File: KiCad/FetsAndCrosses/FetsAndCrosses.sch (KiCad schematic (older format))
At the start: 0 parts

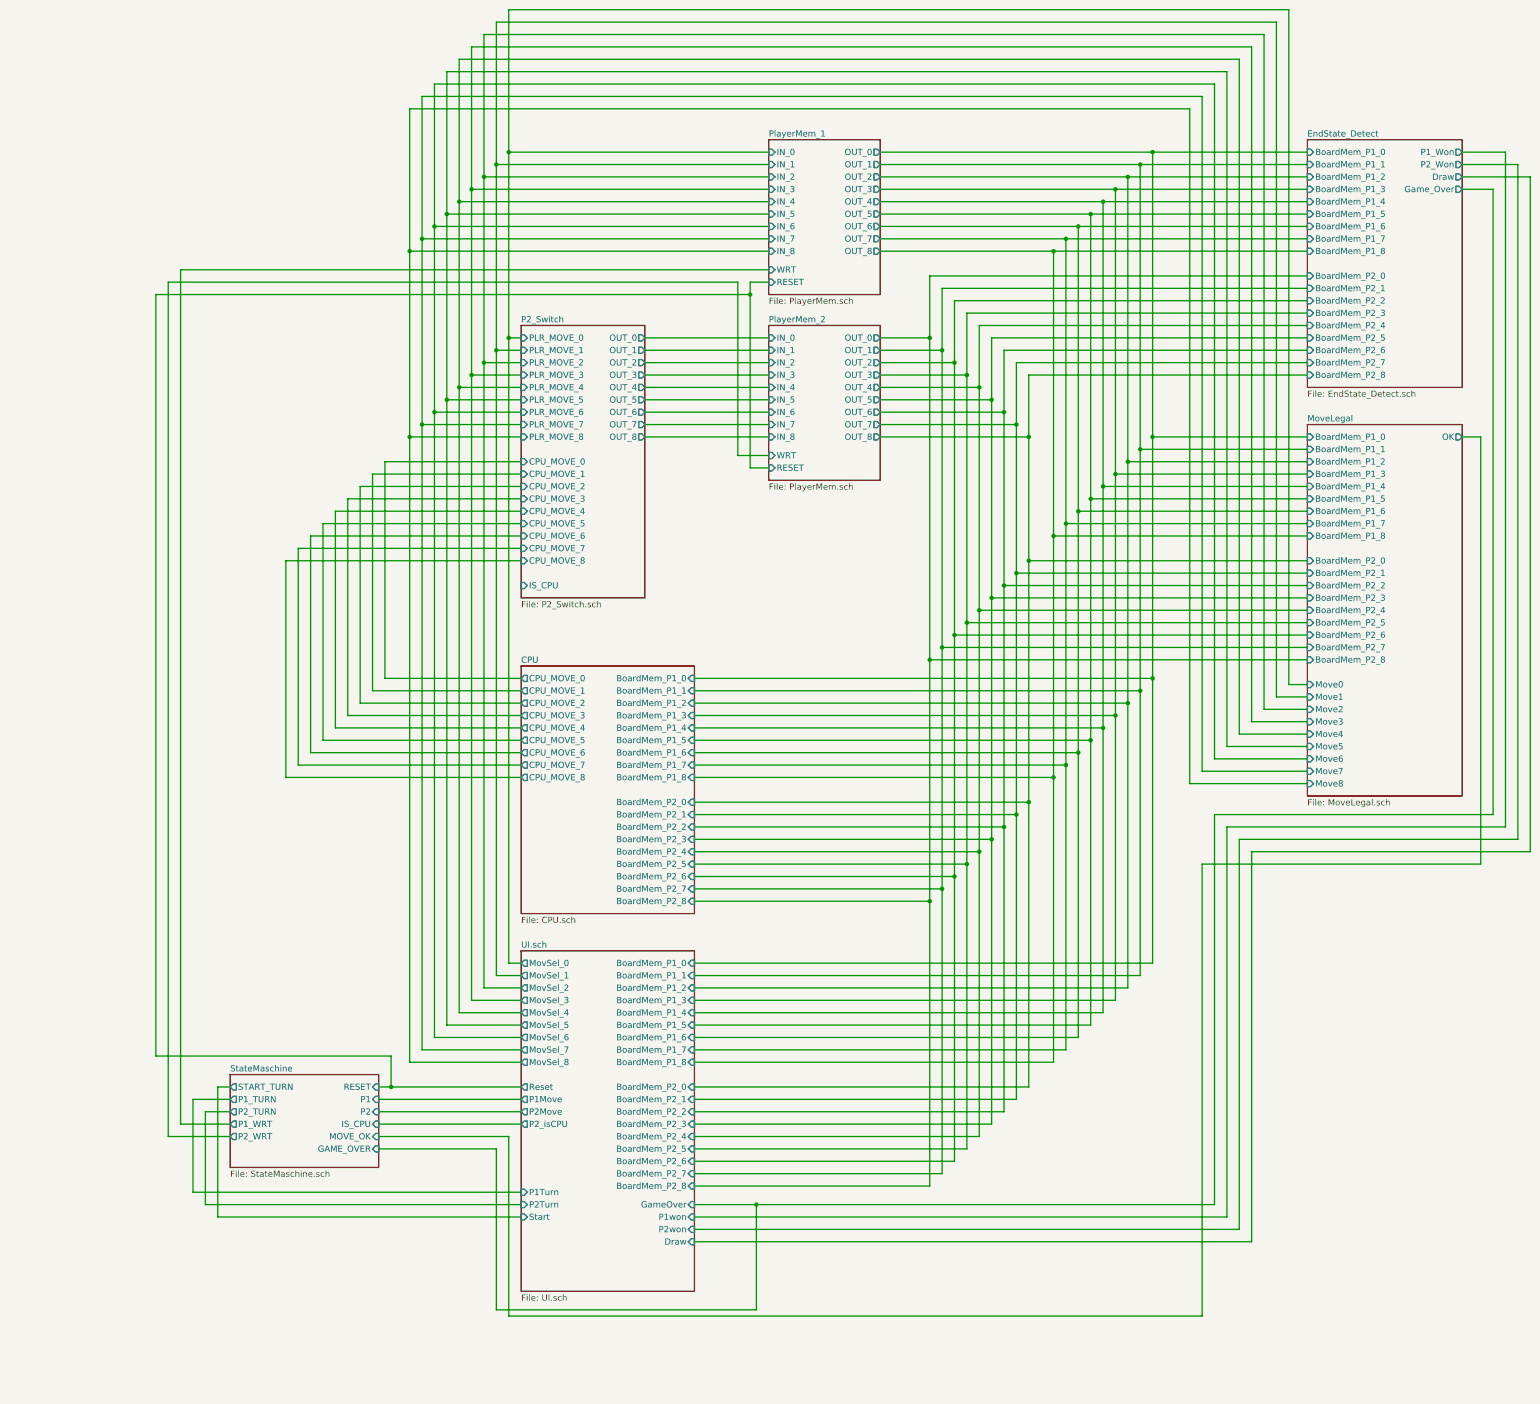
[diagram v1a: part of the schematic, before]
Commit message: Reworked everything to use Buses
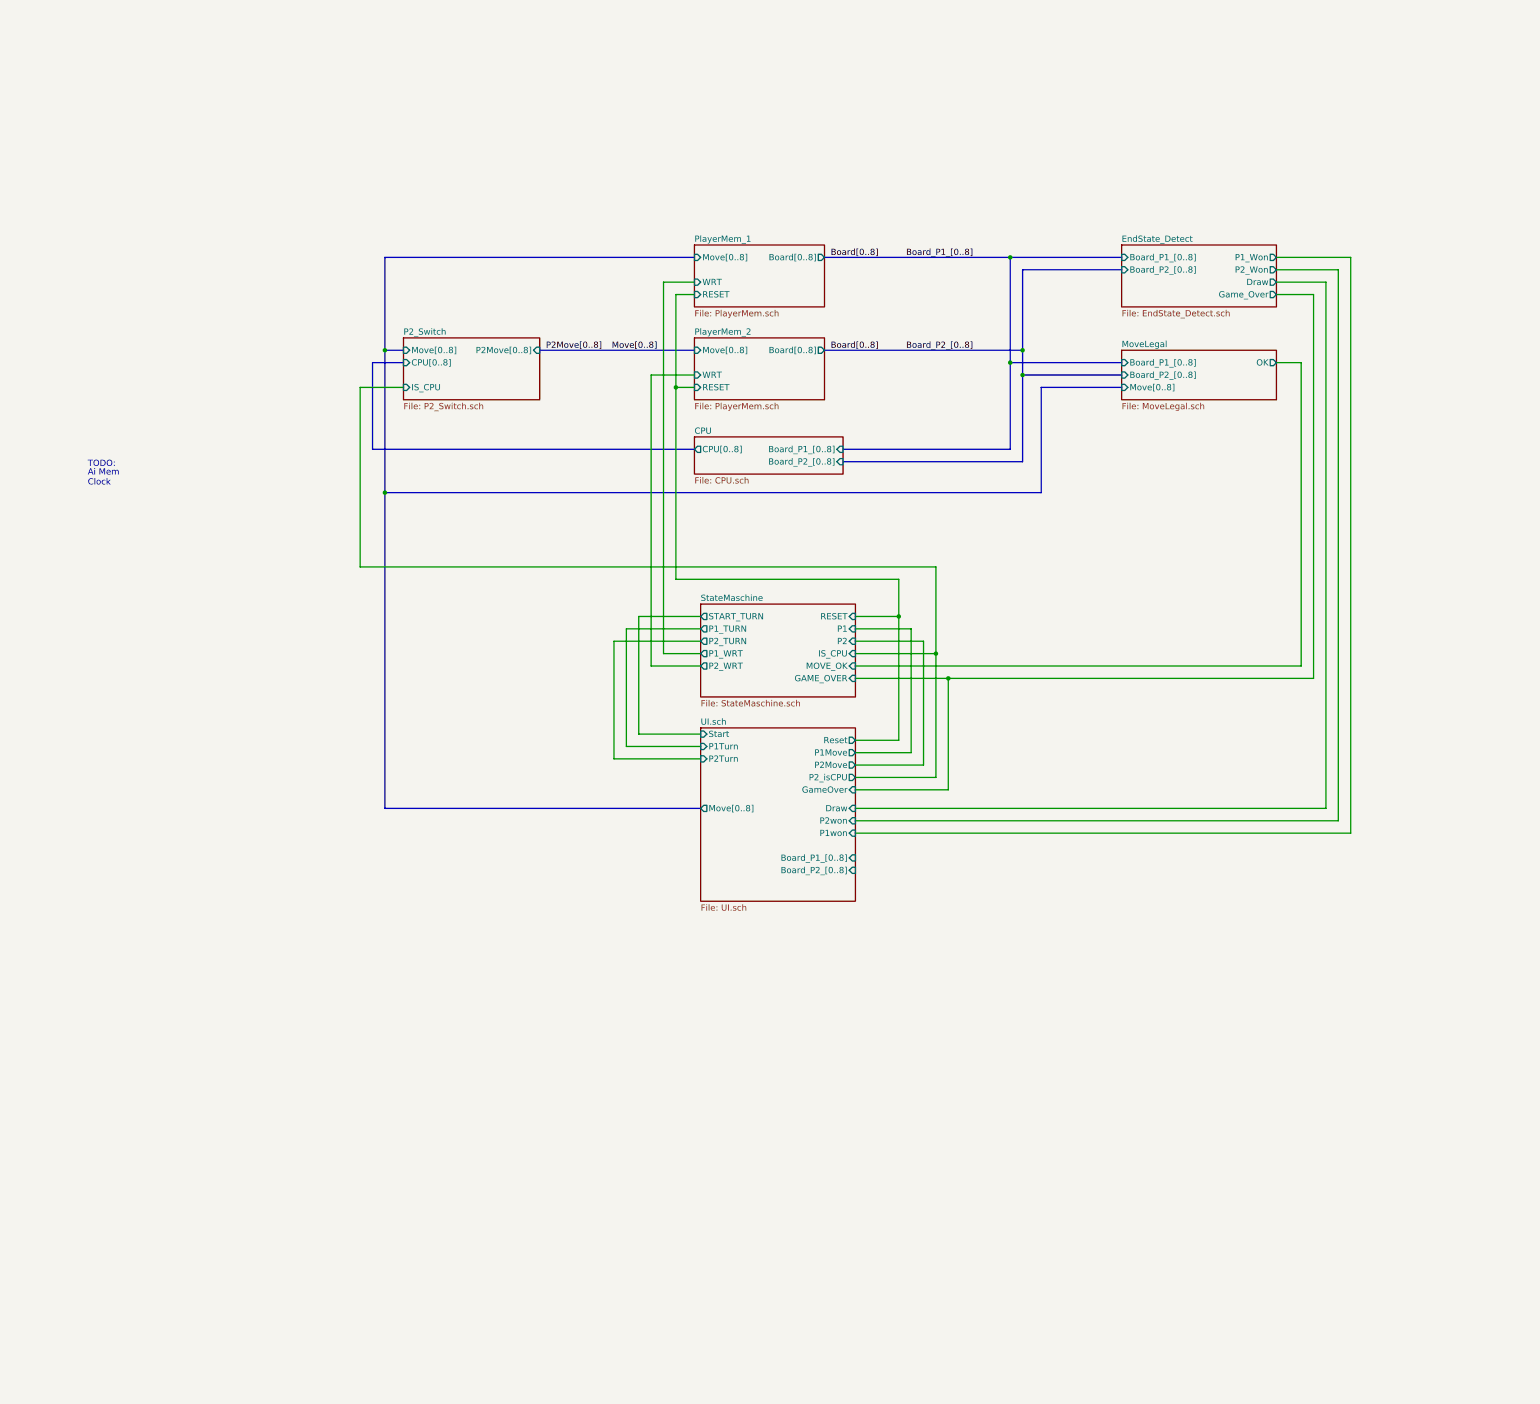
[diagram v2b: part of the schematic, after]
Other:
- note added: "Ai Mem\nClock"
- note added: "TODO:"

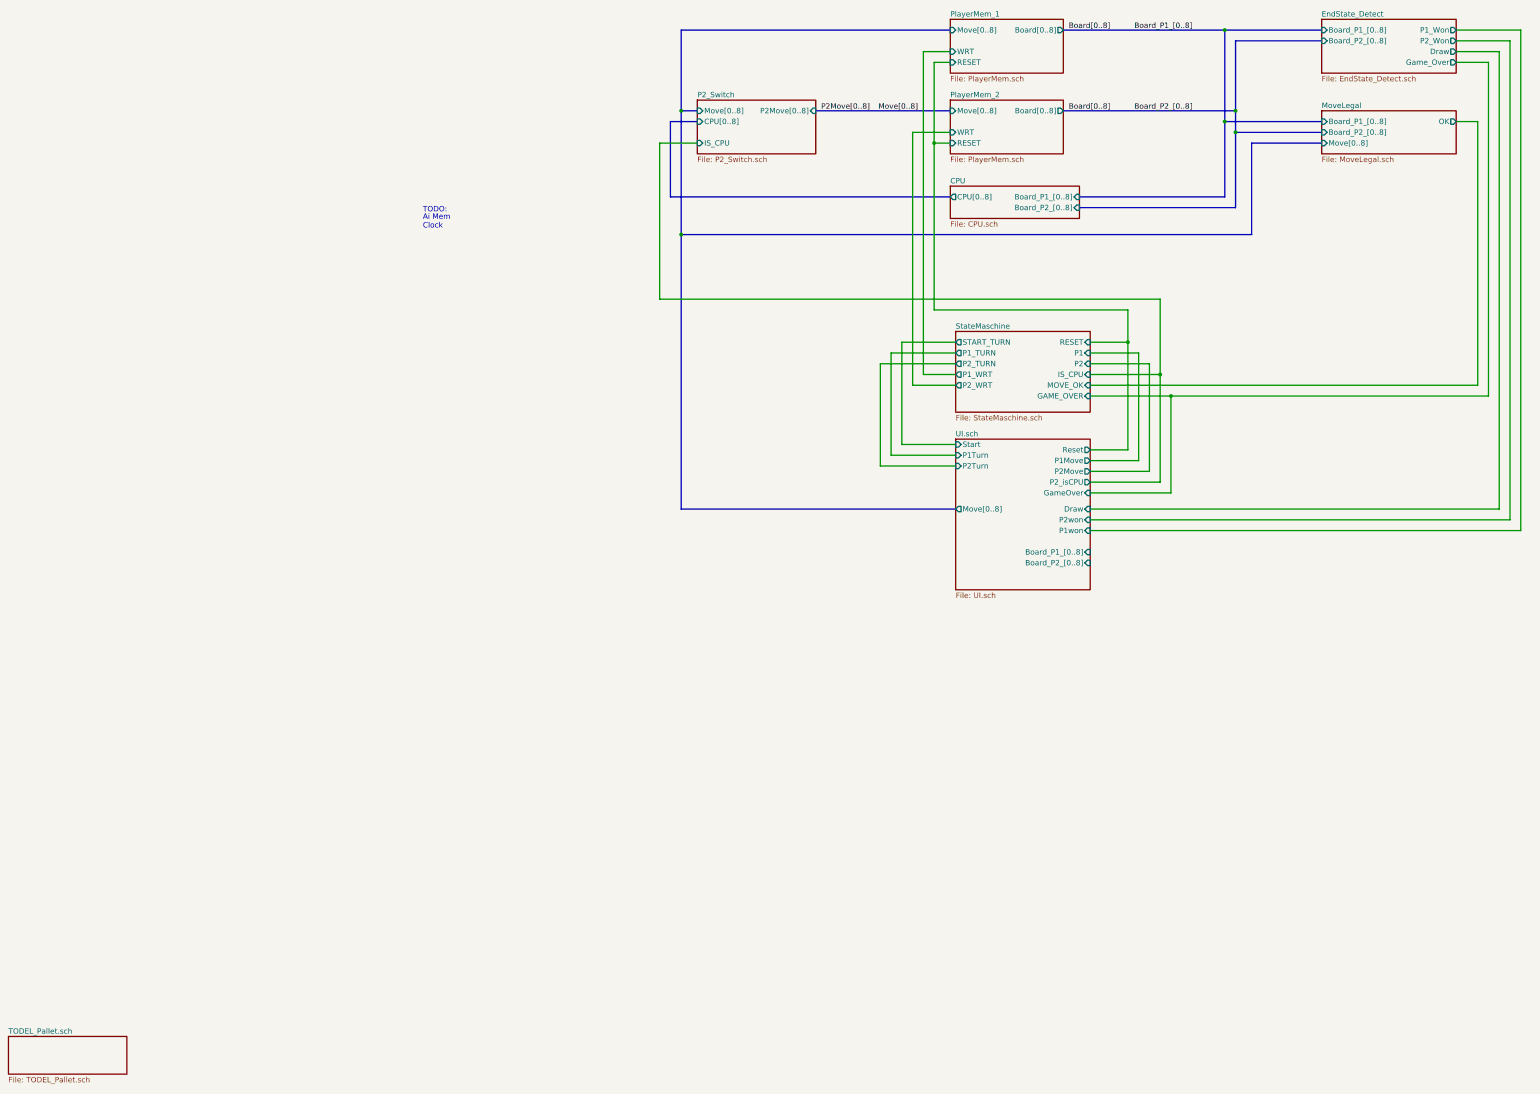
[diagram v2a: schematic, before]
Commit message: Schematic Done, Footprints assigned, ERC OK.
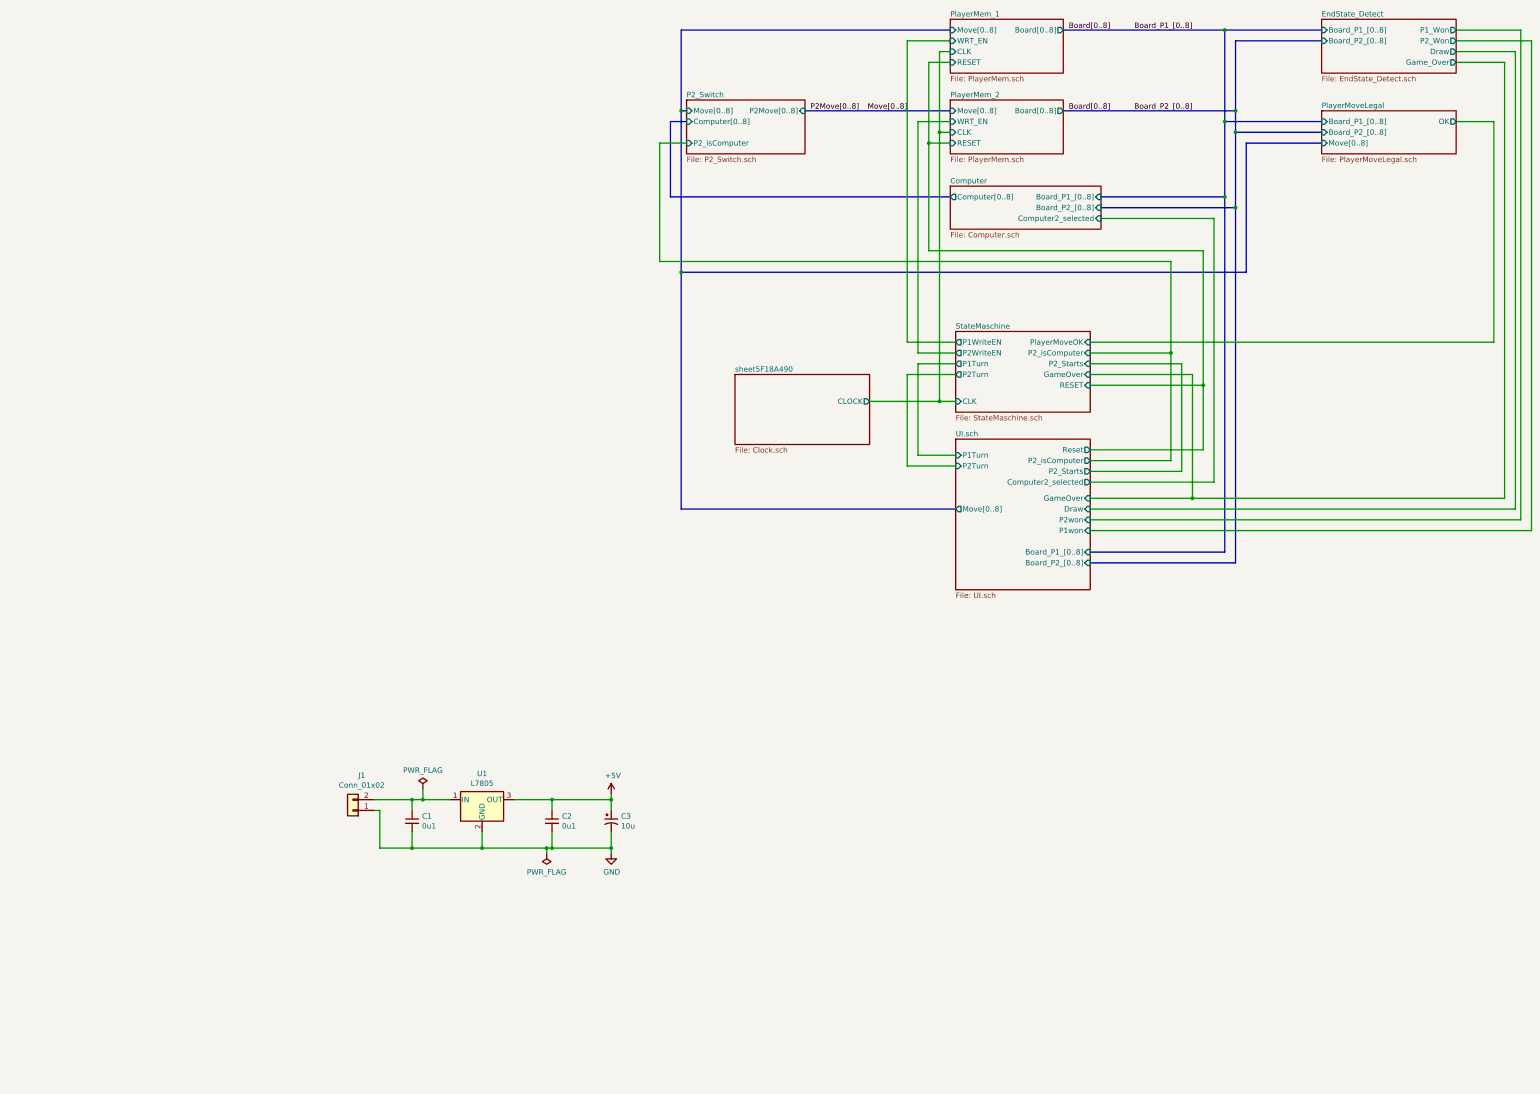
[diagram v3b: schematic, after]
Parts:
- added C1, C2: 0u1, Capacitor_SMD:C_0603_1608Metric, symbol Device:C_Small
- added C3: 10u, Capacitor_SMD:CP_Elec_6.3x7.7, symbol Device:CP1_Small
- added J1: Conn_01x02, Connector_PinHeader_2.54mm:PinHeader_1x02_P2.54mm_Horizontal, symbol Connector_Generic:Conn_01x02
- added U1: L7805, Package_TO_SOT_SMD:TO-252-2, symbol Regulator_Linear:L7805
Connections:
- new net: C1.1, J1.2 (Pin_2), U1.1 (IN)
- new net +5V: C2.1, C3.1, U1.3 (OUT)
- new net GND: C1.2, C2.2, C3.2, J1.1 (Pin_1), U1.2 (GND)
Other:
- note removed: "Ai Mem\nClock"
- note removed: "TODO:"

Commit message: Schematic fixes.
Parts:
- removed J1: Conn_01x02, Connector_PinHeader_2.54mm:PinHeader_1x02_P2.54mm_Horizontal, symbol Connector_Generic:Conn_01x02
- added C10, C11, C12, C13, C14, C15, C16, C17, C18, C19, C20, C21, C22, C23, C24, C25, C26, C9: 0u1, LogicQ:C_0603_1608Metric_NOLBL, symbol Device:C_Small
- added G1: BarrelPolarity_CenterNeg, BarrelPolarity_3mm:BarrelPolarity_3mm_CenterNeg, symbol BarrelPolarity:BarrelPolarity_CenterNeg
- added H1, H2: MountingHole, MountingHole:MountingHole_3.2mm_M3_Pad_Via, symbol Mechanical:MountingHole
- added J1: 9Vdc, Connector_BarrelJack:BarrelJack_Horizontal, symbol Connector:Barrel_Jack
- C1, C2: footprint Capacitor_SMD:C_0603_1608Metric -> LogicQ:C_0603_1608Metric_NOLBL
- C3: footprint Capacitor_SMD:CP_Elec_6.3x7.7 -> Capacitor_Tantalum_SMD:CP_EIA-6032-15_Kemet-U
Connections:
- net +5V: now also C10.1, C11.1, C12.1, C13.1, C14.1, C15.1, C16.1, C17.1, C18.1, C19.1, C20.1, C21.1, C22.1, C23.1, C24.1, C25.1, C26.1, C9.1
- net GND: now also C10.2, C11.2, C12.2, C13.2, C14.2, C15.2, C16.2, C17.2, C18.2, C19.2, C20.2, C21.2, C22.2, C23.2, C24.2, C25.2, C26.2, C9.2, J1.1
- net at C1.1, U1.1 (IN): now also J1.2

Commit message: First Draft Schematic Updates
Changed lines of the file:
@@
 $Descr A3 16535 11693
 encoding utf-8
-Sheet 1 389
+Sheet 1 360
 Title "Fets and Crosses"
 Date "2020-07-05"
@@
 S 5200 5800 1250 650
 U 5F18A492
-F0 "sheet5F18A490" 50
+F0 "Clock" 50
 F1 "Clock.sch" 50
 F2 "CLOCK" O R 6450 6050 50

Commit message: First Layout draft done.
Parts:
- added C? (x4): 0u1, LogicQ:C_0603_1608Metric_NOLBL, symbol Device:C_Small
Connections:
- net +5V: now also C?.1, C?.1, C?.1, C?.1
- net GND: now also C?.2, C?.2, C?.2, C?.2
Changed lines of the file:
@@
 Connection ~ 4550 9750
 Wire Wire Line
-	4550 9750 4900 9750
+	4550 9750 4800 9750
 Wire Wire Line
 	4550 10050 4550 10200
 Connection ~ 4550 10200
 Wire Wire Line
-	4550 10200 4900 10200
+	4550 10200 4700 10200
 Wire Wire Line
 	4900 10050 4900 10200
@@
 	8750 10050 8750 10200
 Connection ~ 8400 10200
+$Comp
+L Device:C_Small C?
+U 1 1 5F52D30B
+P 4900 10500
+F 0 "C?" H 4992 10546 50  0000 L CNN
+F 1 "0u1" H 4992 10455 50  0000 L CNN
+F 2 "LogicQ:C_0603_1608Metric_NOLBL" H 4900 10500 50  0001 C CNN
+F 3 "~" H 4900 10500 50  0001 C CNN
+	1    4900 10500
+	1    0    0    -1
+$EndComp
+$Comp
+L Device:C_Small C?
+U 1 1 5F52D311
+P 5250 10500
+F 0 "C?" H 5342 10546 50  0000 L CNN
+F 1 "0u1" H 5342 10455 50  0000 L CNN
+F 2 "LogicQ:C_0603_1608Metric_NOLBL" H 5250 10500 50  0001 C CNN
+F 3 "~" H 5250 10500 50  0001 C CNN
+	1    5250 10500
+	1    0    0    -1
+$EndComp
+$Comp
+L Device:C_Small C?
+U 1 1 5F52D317
+P 5600 10500
+F 0 "C?" H 5692 10546 50  0000 L CNN
+F 1 "0u1" H 5692 10455 50  0000 L CNN
+F 2 "LogicQ:C_0603_1608Metric_NOLBL" H 5600 10500 50  0001 C CNN
+F 3 "~" H 5600 10500 50  0001 C CNN
+	1    5600 10500
+	1    0    0    -1
+$EndComp
+$Comp
+L Device:C_Small C?
+U 1 1 5F52D31D
+P 5950 10500
+F 0 "C?" H 6042 10546 50  0000 L CNN
+F 1 "0u1" H 6042 10455 50  0000 L CNN
+F 2 "LogicQ:C_0603_1608Metric_NOLBL" H 5950 10500 50  0001 C CNN
+F 3 "~" H 5950 10500 50  0001 C CNN
+	1    5950 10500
+	1    0    0    -1
+$EndComp
+Wire Wire Line
+	5950 10750 5950 10600
+Wire Wire Line
+	5950 10300 5950 10400
+Wire Wire Line
+	5600 10400 5600 10300
+Connection ~ 5600 10300
+Wire Wire Line
+	5600 10300 5950 10300
+Wire Wire Line
+	5250 10400 5250 10300
+Connection ~ 5250 10300
+Wire Wire Line
+	5250 10300 5600 10300
+Wire Wire Line
+	4900 10400 4900 10300
+Wire Wire Line
+	4900 10300 5250 10300
+Wire Wire Line
+	4900 10600 4900 10750
+Wire Wire Line
+	4900 10750 5250 10750
+Wire Wire Line
+	5250 10600 5250 10750
+Connection ~ 5250 10750
+Wire Wire Line
+	5250 10750 5600 10750
+Wire Wire Line
+	5600 10600 5600 10750
+Connection ~ 5600 10750
+Wire Wire Line
+	5600 10750 5950 10750
+Wire Wire Line
+	4900 10300 4800 10300
+Wire Wire Line
+	4800 10300 4800 9750
+Connection ~ 4900 10300
+Connection ~ 4800 9750
+Wire Wire Line
+	4800 9750 4900 9750
+Wire Wire Line
+	4900 10750 4700 10750
+Wire Wire Line
+	4700 10750 4700 10200
+Connection ~ 4900 10750
+Connection ~ 4700 10200
+Wire Wire Line
+	4700 10200 4900 10200
 $EndSCHEMATC

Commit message: Generated Production Files (v0.1)
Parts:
- gave numbers to parts that had none: 4
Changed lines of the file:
@@
 Sheet 1 360
 Title "Fets and Crosses"
-Date "2020-07-05"
-Rev "v0.0"
+Date "2020-08-28"
+Rev "v0.1"
 Comp "Philipp Schilk"
-Comment1 "c"
+Comment1 "Tic-Tac-Toe implementation from discrete-transistor CMOS logic"
 Comment2 ""
 Comment3 ""
-Comment4 ""
+Comment4 "https://github.com/TheSchilk/Fets_and_Crosses"
 $EndDescr
 $Sheet
@@
 Connection ~ 8400 10200
 $Comp
-L Device:C_Small C?
+L Device:C_Small C27
 U 1 1 5F52D30B
 P 4900 10500
-F 0 "C?" H 4992 10546 50  0000 L CNN
+F 0 "C27" H 4992 10546 50  0000 L CNN
 F 1 "0u1" H 4992 10455 50  0000 L CNN
 F 2 "LogicQ:C_0603_1608Metric_NOLBL" H 4900 10500 50  0001 C CNN
@@
 $EndComp
 $Comp
-L Device:C_Small C?
+L Device:C_Small C28
 U 1 1 5F52D311
 P 5250 10500
-F 0 "C?" H 5342 10546 50  0000 L CNN
+F 0 "C28" H 5342 10546 50  0000 L CNN
 F 1 "0u1" H 5342 10455 50  0000 L CNN
 F 2 "LogicQ:C_0603_1608Metric_NOLBL" H 5250 10500 50  0001 C CNN
@@
 $EndComp
 $Comp
-L Device:C_Small C?
+L Device:C_Small C29
 U 1 1 5F52D317
 P 5600 10500
-F 0 "C?" H 5692 10546 50  0000 L CNN
+F 0 "C29" H 5692 10546 50  0000 L CNN
 F 1 "0u1" H 5692 10455 50  0000 L CNN
 F 2 "LogicQ:C_0603_1608Metric_NOLBL" H 5600 10500 50  0001 C CNN
@@
 $EndComp
 $Comp
-L Device:C_Small C?
+L Device:C_Small C30
 U 1 1 5F52D31D
 P 5950 10500
-F 0 "C?" H 6042 10546 50  0000 L CNN
+F 0 "C30" H 6042 10546 50  0000 L CNN
 F 1 "0u1" H 6042 10455 50  0000 L CNN
 F 2 "LogicQ:C_0603_1608Metric_NOLBL" H 5950 10500 50  0001 C CNN
